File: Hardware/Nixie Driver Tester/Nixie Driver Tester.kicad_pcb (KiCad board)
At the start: 4 copper layers, 57.1 x 45.1 mm, 33 parts, among them J1 OLED, J2 SWD, J3 UJC-HP-3-SMT-TR, Q1 MMBT2222A, Q2 MMBT2907ALT1G, Q3 FDD7N25LZTM, SW1 SW_Omron_B3FS, U1 STM32L011F4Ux, U2 HUSB238, U3 TPS62177DQC

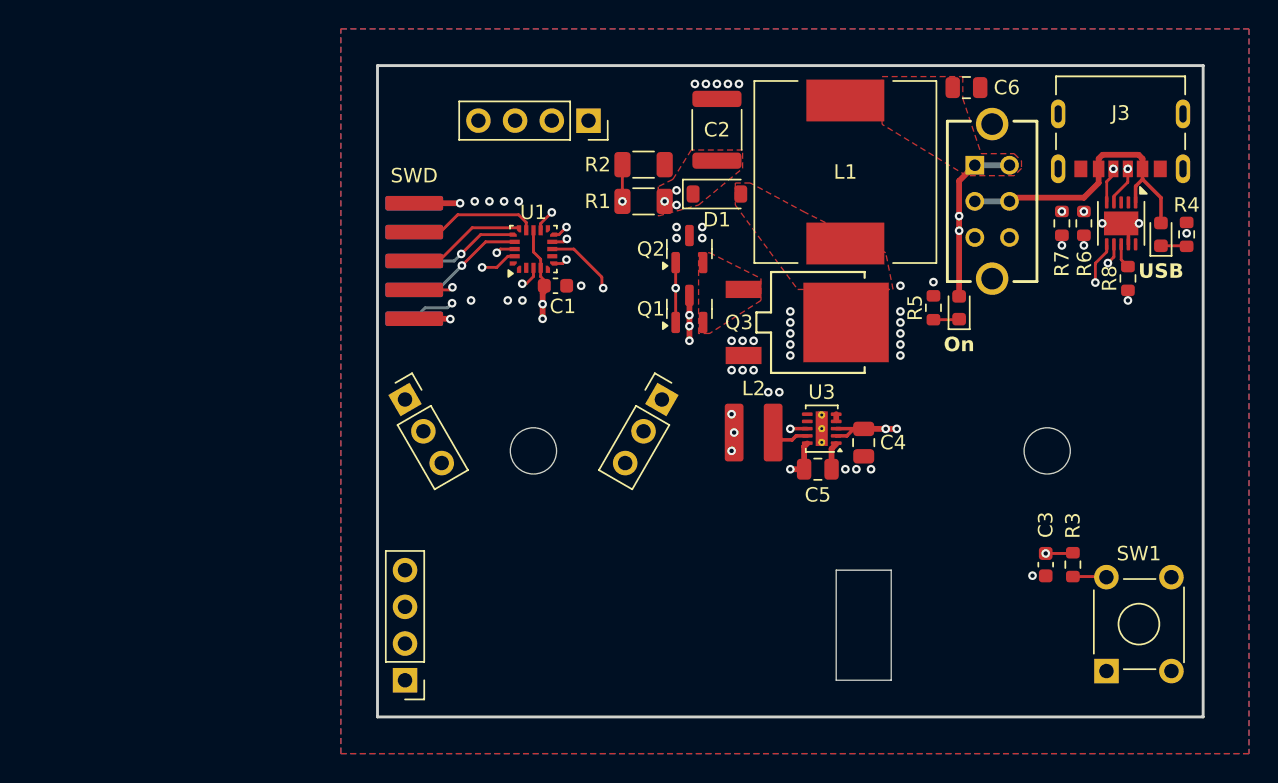
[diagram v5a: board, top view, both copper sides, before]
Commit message: Added test points
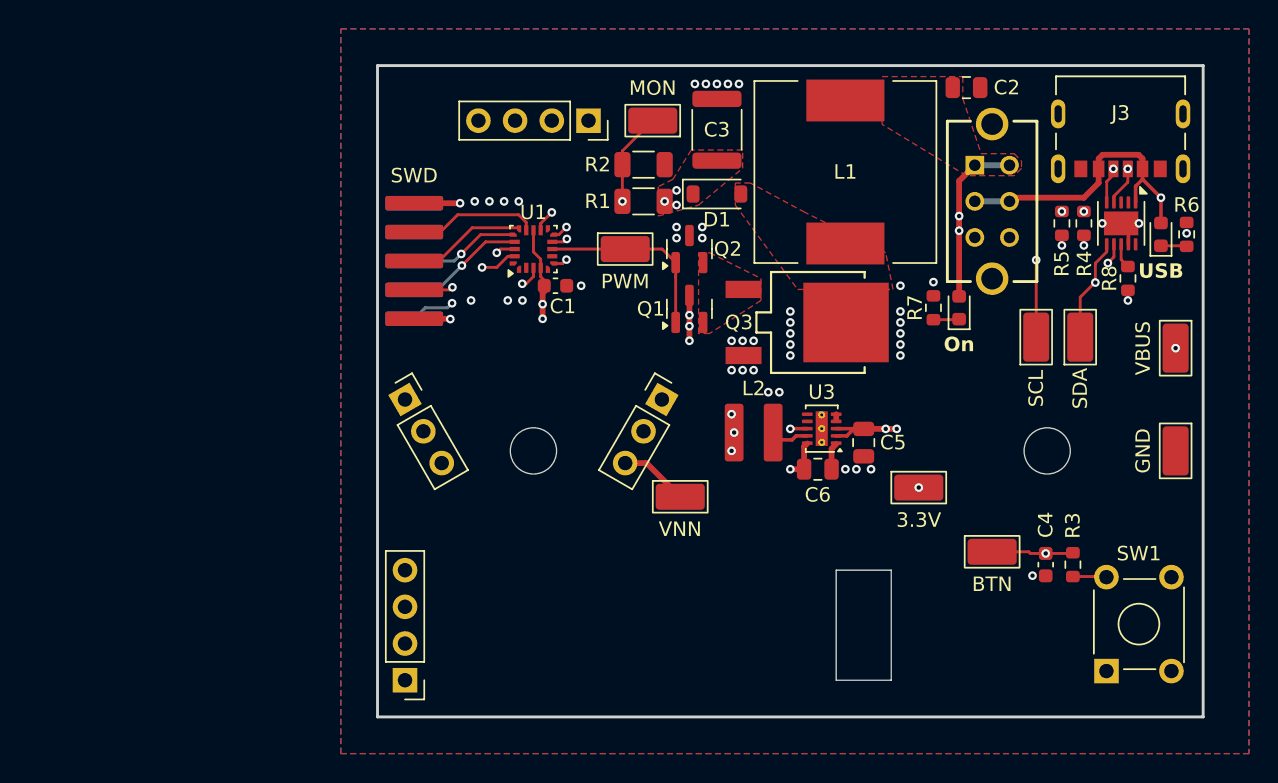
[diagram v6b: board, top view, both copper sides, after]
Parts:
- added TP1: SCL, TestPoint:TestPoint_Keystone_5015_Micro_Mini, F.Cu at (169.4, 97.5)
- added TP2: SDA, TestPoint:TestPoint_Keystone_5015_Micro_Mini, F.Cu at (172.5, 97.5)
- added TP3: PWM, TestPoint:TestPoint_Keystone_5015_Micro_Mini, F.Cu at (141.0, 91.4)
- added TP4: VNN, TestPoint:TestPoint_Keystone_5015_Micro_Mini, F.Cu at (144.8, 108.6)
- added TP5: MON, TestPoint:TestPoint_Keystone_5015_Micro_Mini, F.Cu at (142.9, 82.5)
- added TP6: BTN, TestPoint:TestPoint_Keystone_5015_Micro_Mini, F.Cu at (166.4, 112.4)
- added TP7: GND, TestPoint:TestPoint_Keystone_5015_Micro_Mini, F.Cu at (179.1, 105.4)
- added TP8: VBUS, TestPoint:TestPoint_Keystone_5015_Micro_Mini, F.Cu at (179.1, 98.3)
- added TP9: 3.3V, TestPoint:TestPoint_Keystone_5015_Micro_Mini, F.Cu at (161.3, 108.0)
- renumbered C6 to C2, C2 to C3, C3 to C4, C4 to C5, C5 to C6, R6 to R4, R7 to R5, R4 to R6, R5 to R7
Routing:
- net /USB PD/VBUS In: track 20.8 -> 31.7 mm, vias 0 -> 2
- net /VCC VRM/V_Out: track 82.0 -> 92.5 mm, vias 11 -> 12
- net /Controller/SCL: track 73.2 -> 79.3 mm, vias 2 -> 3
- net /Controller/SDA: track 72.6 -> 77.6 mm
- net /Boost Converter/180V: track 21.3 -> 26.1 mm
- net /Controller/HVMON: track 8.18 -> 12.1 mm
- net /Button/Button: track 51.2 -> 55.0 mm
- net /Boost Converter/PWM: track 14.3 -> 13.1 mm, vias 2 -> 0

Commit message: TP / Trace adjustments
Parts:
- turned TP6 to 180 degrees
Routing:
- net /Controller/SCL: track 79.3 -> 78.5 mm
- net /Button/Button: track 55.0 -> 54.5 mm
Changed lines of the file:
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@@
 	(footprint "TestPoint:TestPoint_Keystone_5015_Micro_Mini"
 		(layer "F.Cu")
-		(at 166.37 112.395)
+		(at 166.37 112.395 180)
 		(descr "Keystone SMT Micro Mini Test Point 5015, http://www.keyelco.com/product-pdf.cfm?p=1353")
 		(tags "Test Point")
@@
 		)
 		(property "Datasheet" ""
-			(at 0 0 0)
+			(at 0 0 180)
 			(unlocked yes)
 			(layer "F.Fab")
@@
 		)
 		(property "Description" "test point"
-			(at 0 0 0)
+			(at 0 0 180)
 			(unlocked yes)
 			(layer "F.Fab")
@@
 		)
 		(fp_line
-			(start -2.15 -1.35)
-			(end 2.15 -1.35)
+			(start 2.15 1.35)
+			(end -2.15 1.35)
 			(stroke
 				(width 0.05)
@@
 		)
 		(fp_line
-			(start -2.15 1.35)
-			(end -2.15 -1.35)
+			(start 2.15 -1.35)
+			(end 2.15 1.35)
 			(stroke
 				(width 0.05)
@@
 		)
 		(fp_line
-			(start 2.15 -1.35)
-			(end 2.15 1.35)
+			(start -2.15 1.35)
+			(end -2.15 -1.35)
 			(stroke
 				(width 0.05)
@@
 		)
 		(fp_line
-			(start 2.15 1.35)
-			(end -2.15 1.35)
+			(start -2.15 -1.35)
+			(end 2.15 -1.35)
 			(stroke
 				(width 0.05)
@@
 		)
 		(pad "1" smd roundrect
-			(at 0 0)
+			(at 0 0 180)
 			(size 3.4 1.8)
 			(layers "F.Cu" "F.Mask" "F.Paste")
@@
 	)
 	(segment
-		(start 169.418 98.298)
-		(end 169.418 92.202)
+		(start 174.8 91.986529)
+		(end 174.8 91.112)
 		(width 0.2)
 		(layer "F.Cu")
@@
 	)
 	(segment
-		(start 174.8 91.986529)
-		(end 174.8 91.112)
+		(start 169.418 92.71)
+		(end 169.418 97.536)
+		(width 0.2)
+		(layer "F.Cu")
+		(net "/Controller/SCL")
+	)
+	(segment
+		(start 169.672 92.456)
+		(end 169.418 92.71)
 		(width 0.2)
 		(layer "F.Cu")
@@
 	)
 	(via
-		(at 169.418 92.202)
+		(at 169.672 92.456)
 		(size 0.6)
 		(drill 0.3)
@@
 	)
 	(segment
-		(start 135.95 92.77)
-		(end 134.874 91.694)
-		(width 0.2)
-		(layer "In1.Cu")
-		(net "/Controller/SCL")
-	)
-	(segment
-		(start 169.418 92.202)
-		(end 168.402 92.202)
+		(start 162.957373 92.964)
+		(end 138.43 92.964)
 		(width 0.2)
 		(layer "In1.Cu")
@@
 	)
 	(segment
-		(start 137.861529 92.063)
-		(end 137.154529 92.77)
+		(start 174.330529 92.456)
+		(end 169.672 92.456)
 		(width 0.2)
 		(layer "In1.Cu")
@@
 	)
 	(segment
-		(start 168.402 92.202)
-		(end 167.099255 92.202)
-		(width 0.2)
-		(layer "In1.Cu")
-		(net "/Controller/SCL")
-	)
-	(segment
-		(start 174.316351 92.202)
-		(end 169.418 92.202)
-		(width 0.2)
-		(layer "In1.Cu")
-		(net "/Controller/SCL")
-	)
-	(segment
-		(start 166.960255 92.063)
-		(end 137.861529 92.063)
+		(start 169.279 92.063)
+		(end 163.858373 92.063)
 		(width 0.2)
 		(layer "In1.Cu")
@@
 	(segment
 		(start 174.380206 92.406323)
-		(end 174.380206 92.265855)
+		(end 174.330529 92.456)
 		(width 0.2)
 		(layer "In1.Cu")
@@
 	)
 	(segment
-		(start 134.874 91.694)
-		(end 132.08 91.694)
+		(start 138.43 92.964)
+		(end 137.16 91.694)
 		(width 0.2)
 		(layer "In1.Cu")
@@
 	)
 	(segment
-		(start 137.154529 92.77)
-		(end 135.95 92.77)
+		(start 137.16 91.694)
+		(end 132.08 91.694)
 		(width 0.2)
 		(layer "In1.Cu")
@@
 	)
 	(segment
-		(start 174.380206 92.265855)
-		(end 174.316351 92.202)
+		(start 163.858373 92.063)
+		(end 162.957373 92.964)
 		(width 0.2)
 		(layer "In1.Cu")
@@
 	)
 	(segment
-		(start 167.099255 92.202)
-		(end 166.960255 92.063)
+		(start 169.672 92.456)
+		(end 169.279 92.063)
 		(width 0.2)
 		(layer "In1.Cu")
@@
 	)
 	(segment
-		(start 169.024 112.509)
-		(end 168.91 112.395)
+		(start 136.636 92.44)
+		(end 136.095 92.44)
 		(width 0.2)
 		(layer "F.Cu")
@@
 	)
 	(segment
-		(start 170.078 112.509)
-		(end 169.024 112.509)
+		(start 136.906 92.964)
+		(end 136.906 92.71)
 		(width 0.2)
 		(layer "F.Cu")
@@
 	)
 	(segment
-		(start 136.636 92.44)
-		(end 136.906 92.17)
+		(start 169.024 112.509)
+		(end 168.91 112.395)
+		(width 0.2)
+		(layer "F.Cu")
+		(net "/Button/Button")
+	)
+	(segment
+		(start 170.078 112.509)
+		(end 169.024 112.509)
 		(width 0.2)
 		(layer "F.Cu")
@@
 	)
 	(segment
-		(start 171.908 112.509)
-		(end 171.958 112.459)
+		(start 136.906 92.71)
+		(end 136.636 92.44)
 		(width 0.2)
 		(layer "F.Cu")
@@
 	)
 	(segment
-		(start 136.095 92.44)
-		(end 136.636 92.44)
+		(start 171.908 112.509)
+		(end 171.958 112.459)
 		(width 0.2)
 		(layer "F.Cu")
@@
 	)
 	(via
-		(at 136.906 92.17)
+		(at 136.906 92.964)
 		(size 0.6)
 		(drill 0.3)
@@
 	)
 	(segment
-		(start 170.078 112.509)
-		(end 145.599245 112.509)
+		(start 145.599245 112.509)
+		(end 170.078 112.509)
 		(width 0.2)
 		(layer "In2.Cu")
@@
 	)
 	(segment
-		(start 145.599245 112.509)
+		(start 136.906 92.964)
 		(end 136.906 103.815755)
 		(width 0.2)
@@
 	(segment
 		(start 136.906 103.815755)
-		(end 136.906 92.17)
+		(end 145.599245 112.509)
 		(width 0.2)
 		(layer "In2.Cu")
@@
 	)
 	(zone
-		(net "/Button/Button")
-		(layer "F.Cu")
-		(hatch none 0.1)
-		(priority 30005)
-		(attr
-			(teardrop
-				(type padvia)
-			)
-		)
-		(connect_pads yes
-			(clearance 0)
-		)
-		(min_thickness 0.0254)
-		(fill yes
-			(island_removal_mode 1)
-		)
-		(polygon
-			(pts
-				(xy 171.003 112.609) (xy 171.003 112.409) (xy 170.414104 112.076127) (xy 170.077 112.509) (xy 170.414104 112.941873)
-			)
-		)
-	)
-	(zone
 		(net "/Boost Converter/VBUS")
 		(layer "F.Cu")
@@
 			)
 		)
-	)
-	(zone
-		(net "/Button/Button")
-		(layer "F.Cu")
-		(hatch none 0.1)
-		(priority 30006)
-		(attr
-			(teardrop
-				(type padvia)
-			)
-		)
-		(connect_pads yes
-			(clearance 0)
-		)
-		(min_thickness 0.0254)
-		(fill yes
-			(island_removal_mode 1)
-		)
-		(polygon
-			(pts
-				(xy 169.153 112.409) (xy 169.153 112.609) (xy 169.741896 112.941873) (xy 170.079 112.509) (xy 169.741896 112.076127)
-			)
-		)
